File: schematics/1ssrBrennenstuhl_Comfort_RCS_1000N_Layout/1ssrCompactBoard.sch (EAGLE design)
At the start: 20 parts, among them K1 AQG12105

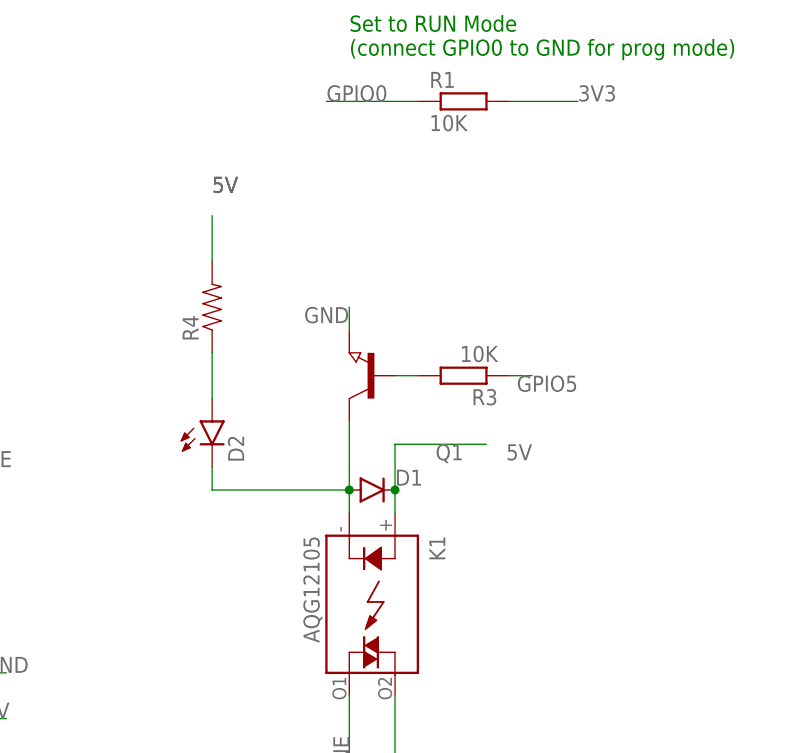
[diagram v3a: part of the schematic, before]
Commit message: diode moved
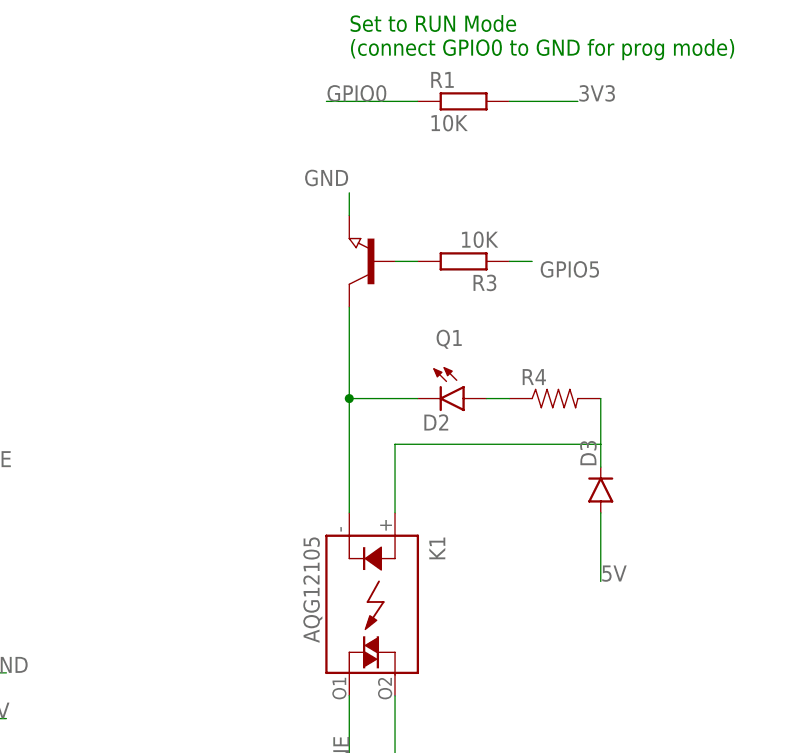
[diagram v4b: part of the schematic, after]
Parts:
- removed D1: (no value), SparkFun-DiscreteSemi:DIODESMA
- added D3: (no value), SparkFun-DiscreteSemi:DIODESMA
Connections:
- new net N$3: D3.C, K1.A, R4.2
- net 5V: now also D3.A; no longer D1.C, K1.A, R4.2
- net N$10: no longer D1.A
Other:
- moved on the sheet: D2, Q1, R3, R4
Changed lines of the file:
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@@
 <part name="C2" library="SparkFun-Capacitors" deviceset="0.1UF-25V-5%(0603)" device="" value="0.1uF"/>
 <part name="Q1" library="semicon-smd-ipc" deviceset="NPN-TRANSISTOR_" device="SOT23"/>
-<part name="D1" library="SparkFun-DiscreteSemi" deviceset="DIODE" device="SMA"/>
 <part name="MDL1" library="ESP8266-ESP12E" deviceset="ESP8266-12E" device="ESP8266-ESP12E"/>
 <part name="R1" library="resistor" deviceset="R-EU_" device="R0805" value="10K"/>
@@
 <part name="R6" library="resistor" deviceset="R-EU_" device="R0805" value="10K"/>
 <part name="J1" library="SparkFun-Connectors" deviceset="M02" device="PTH3"/>
+<part name="D3" library="SparkFun-DiscreteSemi" deviceset="DIODE" device="SMA"/>
 </parts>
 <sheets>
@@
 <instance part="R2" gate="G$1" x="-17.78" y="38.1"/>
 <instance part="K1" gate="A" x="152.4" y="22.86" rot="R270"/>
-<instance part="R3" gate="G$1" x="162.56" y="48.26" rot="R180"/>
+<instance part="R3" gate="G$1" x="162.56" y="60.96" rot="R180"/>
 <instance part="U$4" gate="G$1" x="71.12" y="10.16"/>
 <instance part="R5" gate="G$1" x="-17.78" y="43.18"/>
@@
 <instance part="C1" gate="G$1" x="78.74" y="-7.62"/>
 <instance part="C2" gate="G$1" x="106.68" y="-7.62"/>
-<instance part="Q1" gate="G$1" x="152.4" y="48.26" rot="R180"/>
-<instance part="D1" gate="G$1" x="152.4" y="35.56"/>
+<instance part="Q1" gate="G$1" x="152.4" y="60.96" rot="R180"/>
 <instance part="MDL1" gate="G$1" x="12.7" y="35.56"/>
 <instance part="R1" gate="G$1" x="162.56" y="78.74"/>
@@
 <instance part="L" gate="P" x="25.4" y="-5.08"/>
 <instance part="OUT" gate="P" x="25.4" y="-12.7"/>
-<instance part="D2" gate="G$1" x="134.62" y="43.18"/>
-<instance part="R4" gate="G$1" x="134.62" y="55.88" rot="R90"/>
+<instance part="D2" gate="G$1" x="162.56" y="45.72" rot="R270"/>
+<instance part="R4" gate="G$1" x="172.72" y="45.72"/>
 <instance part="FUSE" gate="G$1" x="81.28" y="38.1"/>
 <instance part="R6" gate="G$1" x="25.4" y="73.66"/>
 <instance part="J1" gate="G$1" x="2.54" y="71.12"/>
+<instance part="D3" gate="G$1" x="177.8" y="35.56" rot="R90"/>
 </instances>
 <busses>
@@
 <segment>
 <pinref part="Q1" gate="G$1" pin="E"/>
-<wire x1="149.86" y1="53.34" x2="149.86" y2="55.88" width="0.1524" layer="91"/>
-<label x="149.86" y="55.88" size="1.778" layer="95" rot="R180"/>
+<wire x1="149.86" y1="66.04" x2="149.86" y2="68.58" width="0.1524" layer="91"/>
+<label x="149.86" y="71.12" size="1.778" layer="95" rot="R180"/>
 </segment>
 <segment>
@@
 </segment>
 <segment>
-<pinref part="K1" gate="A" pin="A"/>
-<pinref part="D1" gate="G$1" pin="C"/>
-<wire x1="154.94" y1="33.02" x2="154.94" y2="35.56" width="0.1524" layer="91"/>
-<wire x1="154.94" y1="35.56" x2="154.94" y2="40.64" width="0.1524" layer="91"/>
-<wire x1="154.94" y1="40.64" x2="165.1" y2="40.64" width="0.1524" layer="91"/>
-<junction x="154.94" y="35.56"/>
-<label x="170.18" y="40.64" size="1.778" layer="95" rot="R180"/>
-</segment>
-<segment>
-<pinref part="R4" gate="G$1" pin="2"/>
-<wire x1="134.62" y1="60.96" x2="134.62" y2="66.04" width="0.1524" layer="91"/>
-<label x="134.62" y="68.58" size="1.778" layer="95"/>
-<label x="134.62" y="68.58" size="1.778" layer="95"/>
+<pinref part="D3" gate="G$1" pin="A"/>
+<wire x1="177.8" y1="33.02" x2="177.8" y2="25.4" width="0.1524" layer="91"/>
+<label x="177.8" y="25.4" size="1.778" layer="95"/>
 </segment>
 </net>
@@
 <segment>
 <pinref part="R3" gate="G$1" pin="1"/>
-<wire x1="167.64" y1="48.26" x2="170.18" y2="48.26" width="0.1524" layer="91"/>
-<label x="175.26" y="48.26" size="1.778" layer="95" rot="R180"/>
+<wire x1="167.64" y1="60.96" x2="170.18" y2="60.96" width="0.1524" layer="91"/>
+<label x="177.8" y="60.96" size="1.778" layer="95" rot="R180"/>
 </segment>
 </net>
@@
 <segment>
 <pinref part="K1" gate="A" pin="K"/>
-<pinref part="D1" gate="G$1" pin="A"/>
-<wire x1="149.86" y1="33.02" x2="149.86" y2="35.56" width="0.1524" layer="91"/>
+<wire x1="149.86" y1="33.02" x2="149.86" y2="45.72" width="0.1524" layer="91"/>
 <pinref part="Q1" gate="G$1" pin="C"/>
-<wire x1="149.86" y1="43.18" x2="149.86" y2="35.56" width="0.1524" layer="91"/>
-<junction x="149.86" y="35.56"/>
+<wire x1="149.86" y1="55.88" x2="149.86" y2="45.72" width="0.1524" layer="91"/>
+<junction x="149.86" y="45.72"/>
 <pinref part="D2" gate="G$1" pin="C"/>
-<wire x1="134.62" y1="38.1" x2="134.62" y2="35.56" width="0.1524" layer="91"/>
-<wire x1="134.62" y1="35.56" x2="149.86" y2="35.56" width="0.1524" layer="91"/>
+<wire x1="157.48" y1="45.72" x2="149.86" y2="45.72" width="0.1524" layer="91"/>
 </segment>
 </net>
@@
 <pinref part="Q1" gate="G$1" pin="B"/>
 <pinref part="R3" gate="G$1" pin="2"/>
-<wire x1="154.94" y1="48.26" x2="157.48" y2="48.26" width="0.1524" layer="91"/>
+<wire x1="154.94" y1="60.96" x2="157.48" y2="60.96" width="0.1524" layer="91"/>
 </segment>
 </net>
@@
 <pinref part="R4" gate="G$1" pin="1"/>
 <pinref part="D2" gate="G$1" pin="A"/>
-<wire x1="134.62" y1="50.8" x2="134.62" y2="45.72" width="0.1524" layer="91"/>
+<wire x1="167.64" y1="45.72" x2="165.1" y2="45.72" width="0.1524" layer="91"/>
 </segment>
 </net>
@@
 </segment>
 </net>
+<net name="N$3" class="0">
+<segment>
+<pinref part="K1" gate="A" pin="A"/>
+<wire x1="154.94" y1="33.02" x2="154.94" y2="40.64" width="0.1524" layer="91"/>
+<wire x1="154.94" y1="40.64" x2="177.8" y2="40.64" width="0.1524" layer="91"/>
+<pinref part="R4" gate="G$1" pin="2"/>
+<wire x1="177.8" y1="45.72" x2="177.8" y2="40.64" width="0.1524" layer="91"/>
+<pinref part="D3" gate="G$1" pin="C"/>
+<wire x1="177.8" y1="38.1" x2="177.8" y2="40.64" width="0.1524" layer="91"/>
+</segment>
+</net>
